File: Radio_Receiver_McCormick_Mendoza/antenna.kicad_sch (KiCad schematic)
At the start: 30 parts, among them J33 XFIL_IN, J34 XFIL_OUT, J5 Conn_Coaxial, J5 FIL_IN, J8 FIL_OUT, T1 Transformer_1P_SS, U13 SN74CBT3253CDBR

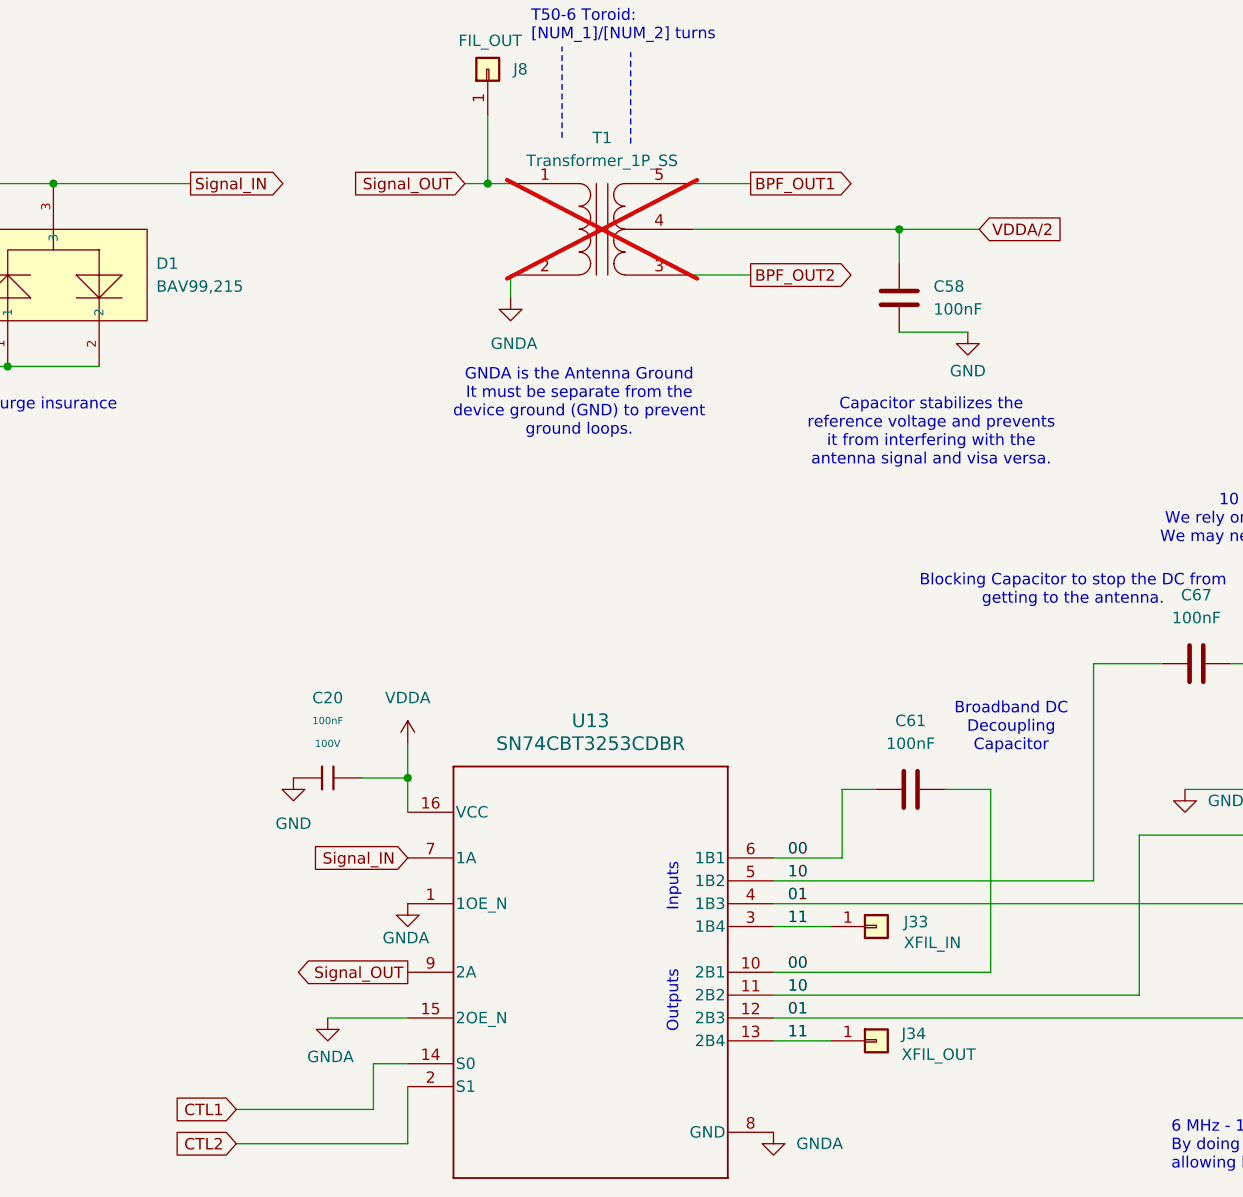
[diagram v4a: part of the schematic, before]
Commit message: Finalized Pico connections and added indicator LEDs
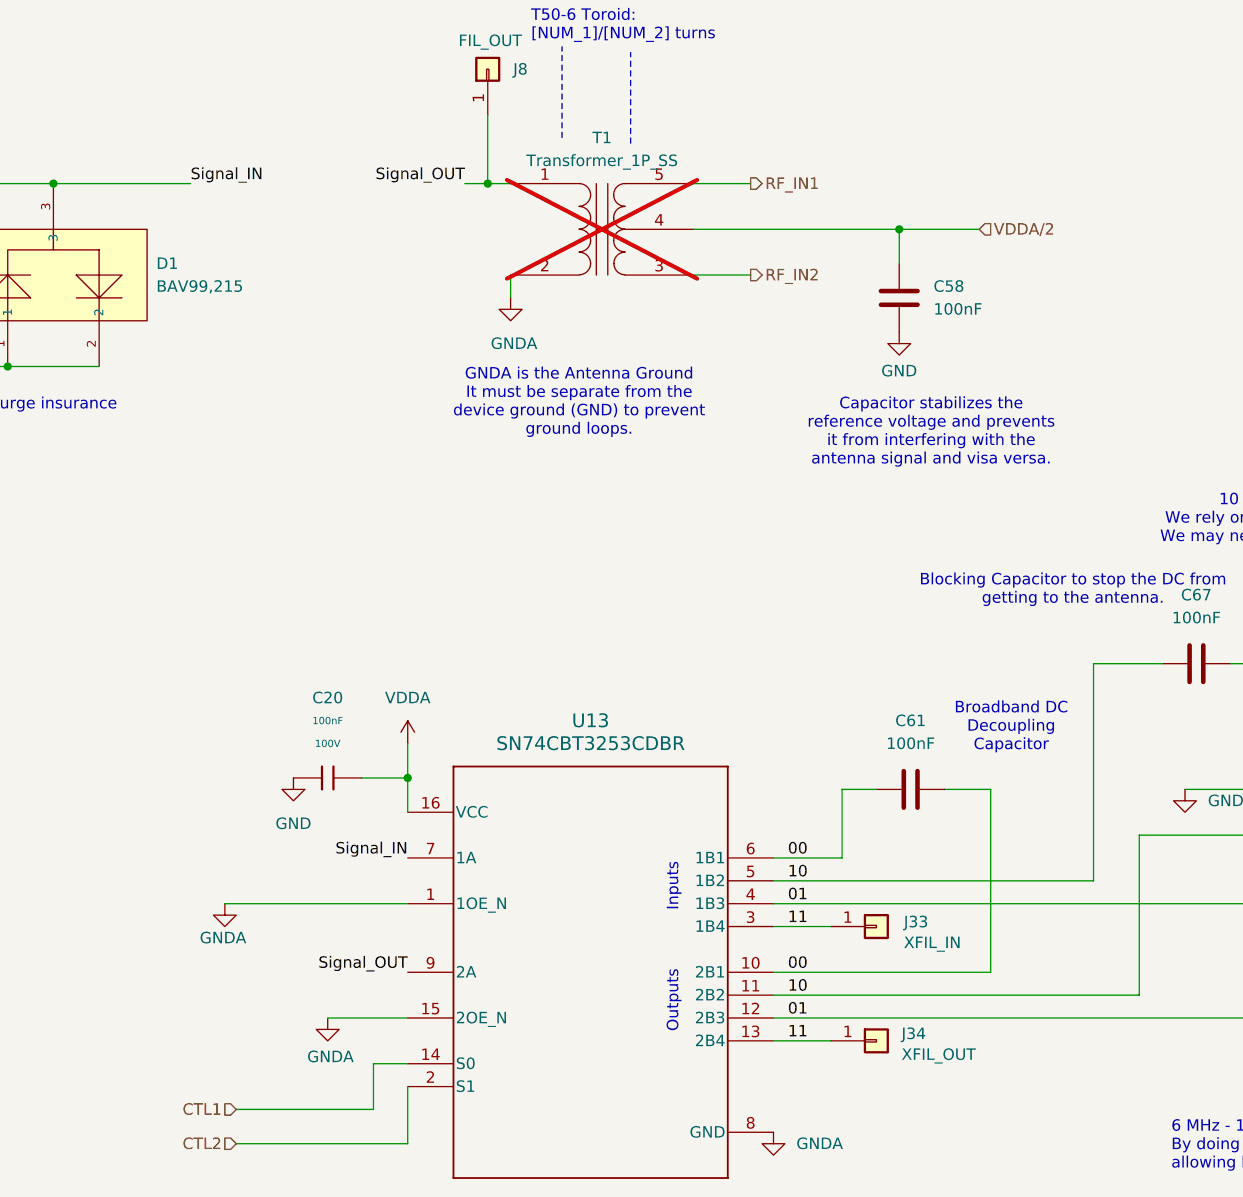
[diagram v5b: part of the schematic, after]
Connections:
- net BPF_OUT1 renamed RF_IN1
- net BPF_OUT2 renamed RF_IN2
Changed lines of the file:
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@@
 	(wire
 		(pts
+			(xy 86.36 120.65) (xy 106.68 120.65)
+		)
+		(stroke
+			(width 0)
+			(type default)
+		)
+	)
+	(wire
+		(pts
 			(xy 106.68 133.35) (xy 97.79 133.35)
 		)
@@
 	(wire
 		(pts
-			(xy 161.29 57.15) (xy 168.91 57.15)
-		)
-		(stroke
-			(width 0)
-			(type default)
-		)
-	)
-	(wire
-		(pts
 			(xy 198.12 93.98) (xy 203.2 93.98)
 		)
@@
 		)
 	)
-	(label "00"
-		(at 151.13 128.27 180)
+	(label "Signal_OUT"
+		(at 106.68 128.27 180)
 		(effects
 			(font
@@
 		)
 	)
-	(label "01"
-		(at 151.13 133.35 180)
+	(label "00"
+		(at 151.13 128.27 180)
 		(effects
 			(font
@@
 		)
 	)
-	(label "11"
-		(at 151.13 135.89 180)
+	(label "01"
+		(at 151.13 133.35 180)
 		(effects
 			(font
@@
 		)
 	)
-	(label "10"
-		(at 151.13 118.11 180)
+	(label "Signal_IN"
+		(at 106.68 115.57 180)
 		(effects
 			(font
@@
 		)
 	)
-	(label "00"
-		(at 151.13 115.57 180)
+	(label "11"
+		(at 151.13 135.89 180)
 		(effects
 			(font
@@
 	)
 	(label "10"
-		(at 151.13 130.81 180)
+		(at 151.13 118.11 180)
 		(effects
 			(font
@@
 		)
 	)
-	(label "01"
-		(at 151.13 120.65 180)
+	(label "00"
+		(at 151.13 115.57 180)
 		(effects
 			(font
@@
 		)
 	)
-	(global_label "CTL2"
-		(shape input)
-		(at 87.63 147.32 180)
-		(fields_autoplaced yes)
-		(effects
-			(font
-				(size 1.27 1.27)
-			)
-			(justify right)
-		)
-		(property "Intersheetrefs" "${INTERSHEET_REFS}"
-			(at 80.1696 147.32 0)
-			(hide yes)
-			(show_name no)
-			(do_not_autoplace no)
-			(effects
-				(font
-					(size 1.27 1.27)
-				)
-				(justify right)
-			)
-		)
-	)
-	(global_label "Signal_IN"
-		(shape input)
-		(at 106.68 115.57 180)
-		(fields_autoplaced yes)
+	(label "Signal_IN"
+		(at 82.55 40.64 0)
 		(effects
 			(font
 				(size 1.27 1.27)
 			)
-			(justify right)
-		)
-		(property "Intersheetrefs" "${INTERSHEET_REFS}"
-			(at 94.8654 115.57 0)
-			(hide yes)
-			(show_name no)
-			(do_not_autoplace no)
-			(effects
-				(font
-					(size 1.27 1.27)
-				)
-				(justify right)
-			)
+			(justify left bottom)
 		)
 	)
-	(global_label "Signal_OUT"
-		(shape input)
+	(label "Signal_OUT"
 		(at 113.03 40.64 180)
-		(fields_autoplaced yes)
 		(effects
 			(font
 				(size 1.27 1.27)
 			)
-			(justify right)
-		)
-		(property "Intersheetrefs" "${INTERSHEET_REFS}"
-			(at 99.5221 40.64 0)
-			(hide yes)
-			(show_name no)
-			(do_not_autoplace no)
-			(effects
-				(font
-					(size 1.27 1.27)
-				)
-				(justify right)
-			)
+			(justify right bottom)
 		)
 	)
-	(global_label "BPF_OUT2"
-		(shape output)
-		(at 144.78 50.8 0)
-		(fields_autoplaced yes)
+	(label "10"
+		(at 151.13 130.81 180)
 		(effects
 			(font
 				(size 1.27 1.27)
 			)
-			(justify left)
-		)
-		(property "Intersheetrefs" "${INTERSHEET_REFS}"
-			(at 157.1995 50.8 0)
-			(hide yes)
-			(show_name no)
-			(do_not_autoplace no)
-			(effects
-				(font
-					(size 1.27 1.27)
-				)
-				(justify left)
-			)
+			(justify right bottom)
 		)
 	)
-	(global_label "Signal_OUT"
-		(shape output)
-		(at 106.68 128.27 180)
-		(fields_autoplaced yes)
+	(label "01"
+		(at 151.13 120.65 180)
 		(effects
 			(font
 				(size 1.27 1.27)
 			)
-			(justify right)
-		)
-		(property "Intersheetrefs" "${INTERSHEET_REFS}"
-			(at 93.1721 128.27 0)
-			(hide yes)
-			(show_name no)
-			(do_not_autoplace no)
-			(effects
-				(font
-					(size 1.27 1.27)
-				)
-				(justify right)
-			)
+			(justify right bottom)
 		)
 	)
-	(global_label "Signal_IN"
+	(hierarchical_label "RF_IN1"
 		(shape output)
-		(at 82.55 40.64 0)
-		(fields_autoplaced yes)
+		(at 144.78 40.64 0)
 		(effects
 			(font
@@
 			(justify left)
 		)
-		(property "Intersheetrefs" "${INTERSHEET_REFS}"
-			(at 94.3646 40.64 0)
-			(hide yes)
-			(show_name no)
-			(do_not_autoplace no)
-			(effects
-				(font
-					(size 1.27 1.27)
-				)
-				(justify left)
-			)
-		)
 	)
-	(global_label "VDDA{slash}2"
+	(hierarchical_label "CTL2"
 		(shape input)
-		(at 170.18 45.72 0)
-		(fields_autoplaced yes)
+		(at 87.63 147.32 180)
 		(effects
 			(font
 				(size 1.27 1.27)
 			)
-			(justify left)
-		)
-		(property "Intersheetrefs" "${INTERSHEET_REFS}"
-			(at 180.4224 45.72 0)
-			(hide yes)
-			(show_name no)
-			(do_not_autoplace no)
-			(effects
-				(font
-					(size 1.27 1.27)
-				)
-				(justify left)
-			)
+			(justify right)
 		)
 	)
-	(global_label "CTL1"
+	(hierarchical_label "CTL1"
 		(shape input)
 		(at 87.63 143.51 180)
-		(fields_autoplaced yes)
 		(effects
 			(font
@@
 			(justify right)
 		)
-		(property "Intersheetrefs" "${INTERSHEET_REFS}"
-			(at 80.1696 143.51 0)
-			(hide yes)
-			(show_name no)
-			(do_not_autoplace no)
-			(effects
-				(font
-					(size 1.27 1.27)
-				)
-				(justify right)
+	)
+	(hierarchical_label "VDDA{slash}2"
+		(shape input)
+		(at 170.18 45.72 0)
+		(effects
+			(font
+				(size 1.27 1.27)
 			)
+			(justify left)
 		)
 	)
-	(global_label "BPF_OUT1"
+	(hierarchical_label "RF_IN2"
 		(shape output)
-		(at 144.78 40.64 0)
-		(fields_autoplaced yes)
+		(at 144.78 50.8 0)
 		(effects
 			(font
@@
 			(justify left)
 		)
-		(property "Intersheetrefs" "${INTERSHEET_REFS}"
-			(at 157.1995 40.64 0)
-			(hide yes)
-			(show_name no)
-			(do_not_autoplace no)
-			(effects
-				(font
-					(size 1.27 1.27)
-				)
-				(justify left)
-			)
-		)
 	)
 	(symbol
@@
 	(symbol
 		(lib_id "power:GND")
-		(at 168.91 57.15 0)
+		(at 161.29 57.15 0)
 		(unit 1)
 		(body_style 1)
@@
 		(dnp no)
 		(property "Reference" "#PWR063"
-			(at 168.91 63.5 0)
+			(at 161.29 63.5 0)
 			(hide yes)
 			(show_name no)
@@
 		)
 		(property "Value" "GND"
-			(at 168.91 61.468 0)
+			(at 161.29 61.468 0)
 			(show_name no)
 			(do_not_autoplace no)
@@
 		)
 		(property "Footprint" ""
-			(at 168.91 57.15 0)
+			(at 161.29 57.15 0)
 			(hide yes)
 			(show_name no)
@@
 		)
 		(property "Datasheet" ""
-			(at 168.91 57.15 0)
+			(at 161.29 57.15 0)
 			(hide yes)
 			(show_name no)
@@
 		)
 		(property "Description" "Power symbol creates a global label with name \"GND\" , ground"
-			(at 168.91 57.15 0)
+			(at 161.29 57.15 0)
 			(hide yes)
 			(show_name no)
@@
 	(symbol
 		(lib_id "power:GND")
-		(at 106.68 120.65 0)
+		(at 86.36 120.65 0)
 		(unit 1)
 		(body_style 1)
@@
 		(dnp no)
 		(property "Reference" "#PWR09"
-			(at 106.68 127 0)
+			(at 86.36 127 0)
 			(hide yes)
 			(show_name no)
@@
 		)
 		(property "Value" "GNDA"
-			(at 103.886 124.46 0)
+			(at 83.566 124.46 0)
 			(show_name no)
 			(do_not_autoplace no)
@@
 		)
 		(property "Footprint" ""
-			(at 106.68 120.65 0)
+			(at 86.36 120.65 0)
 			(hide yes)
 			(show_name no)
@@
 		)
 		(property "Datasheet" ""
-			(at 106.68 120.65 0)
+			(at 86.36 120.65 0)
 			(hide yes)
 			(show_name no)
@@
 		)
 		(property "Description" "Power symbol creates a global label with name \"GND\" , ground"
-			(at 106.68 120.65 0)
+			(at 86.36 120.65 0)
 			(hide yes)
 			(show_name no)

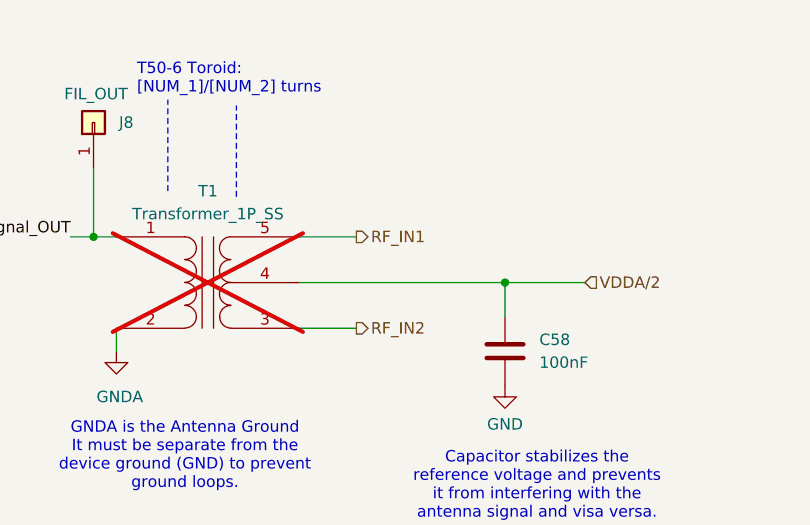
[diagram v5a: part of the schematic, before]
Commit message: Added transformer footprint and datasheet
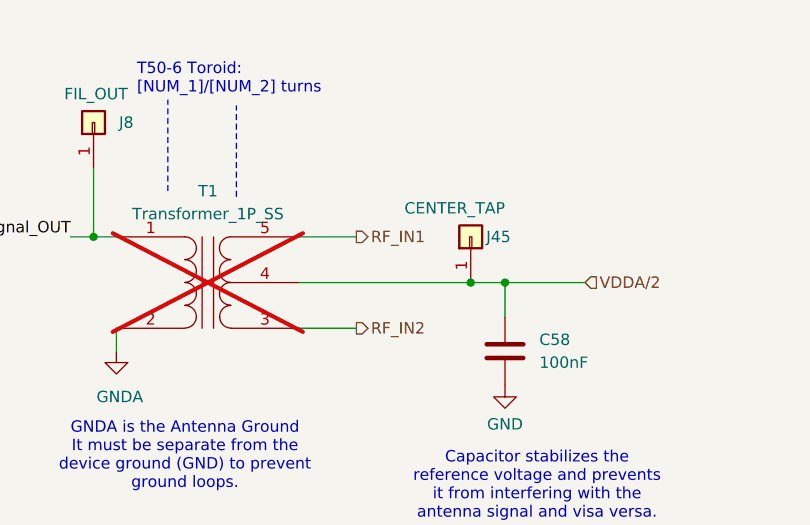
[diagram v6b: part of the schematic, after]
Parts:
- added J45: CENTER_TAP, Connector_PinHeader_2.54mm:PinHeader_1x01_P2.54mm_Vertical, symbol SDRReciever-rescue:Conn_01x01-Connector_Generic-SDRReciever-rescue
- C11, C19, C3, C4: Manufacturer FH(Guangdong Fenghua Advanced Tech) -> (none)
- C2, C22, C30, C31, C51, C53, C54, C55, C87: Manufacturer Samsung Electro-Mechanics -> (none)
- D1: Manufacturer Nexperia -> (none)
- T1: footprint (none) -> Reciever_Parts:Transformer_Toroid_Vertical_2Pri_3Sec_T37
- U13: LCSC (none) -> C2674583; Price (none) -> 3.5033USD
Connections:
- net VDDA/2: now also J45.1 (Pin_1)
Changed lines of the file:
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@@
 	)
 	(junction
+		(at 157.48 45.72)
+		(diameter 0)
+		(color 0 0 0 0)
+	)
+	(junction
 		(at 226.06 133.35)
 		(diameter 0)
@@
 	(wire
 		(pts
+			(xy 157.48 45.72) (xy 161.29 45.72)
+		)
+		(stroke
+			(width 0)
+			(type default)
+		)
+	)
+	(wire
+		(pts
 			(xy 250.19 132.08) (xy 250.19 133.35)
 		)
@@
 	(wire
 		(pts
-			(xy 138.43 45.72) (xy 161.29 45.72)
+			(xy 138.43 45.72) (xy 157.48 45.72)
 		)
 		(stroke
@@
 			)
 		)
-		(property "Footprint" ""
+		(property "Footprint" "Reciever_Parts:Transformer_Toroid_Vertical_2Pri_3Sec_T37"
 			(at 128.27 45.72 0)
 			(hide yes)
@@
 			)
 		)
-		(property "Datasheet" ""
+		(property "Datasheet" "https://www.rf-microwave.com/resources/products_attachments/6128ffba1982b.pdf"
 			(at 128.27 45.72 0)
 			(hide yes)
@@
 			)
 		)
-		(property "Manufacturer" "Samsung Electro-Mechanics"
-			(at 220.98 105.41 0)
-			(hide yes)
-			(show_name no)
-			(do_not_autoplace no)
-			(effects
-				(font
-					(size 1.27 1.27)
-				)
-			)
-		)
 		(property "Part" "CL21C222JBFNNNE"
 			(at 220.98 105.41 0)
@@
 			)
 		)
-		(property "Manufacturer" "FH(Guangdong Fenghua Advanced Tech)"
-			(at 242.57 97.79 0)
-			(hide yes)
-			(show_name no)
-			(do_not_autoplace no)
-			(effects
-				(font
-					(size 1.27 1.27)
-				)
-			)
-		)
 		(property "Part" "0402CG101J500NT"
 			(at 242.57 97.79 0)
@@
 			)
 		)
-		(property "Manufacturer" "Samsung Electro-Mechanics"
-			(at 220.98 97.79 0)
-			(hide yes)
-			(show_name no)
-			(do_not_autoplace no)
-			(effects
-				(font
-					(size 1.27 1.27)
-				)
-			)
-		)
 		(property "Part" "CL21C222JBFNNNE"
 			(at 220.98 97.79 0)
@@
 			)
 		)
-		(property "Manufacturer" "Samsung Electro-Mechanics"
-			(at 261.62 97.79 0)
-			(hide yes)
-			(show_name no)
-			(do_not_autoplace no)
-			(effects
-				(font
-					(size 1.27 1.27)
-				)
-			)
-		)
 		(property "Part" "CL21C222JBFNNNE"
 			(at 261.62 97.79 0)
@@
 			)
 		)
+		(property "LCSC" "C2674583"
+			(at 127 128.27 0)
+			(hide yes)
+			(show_name no)
+			(do_not_autoplace no)
+			(effects
+				(font
+					(size 1.27 1.27)
+				)
+			)
+		)
+		(property "Price" "3.5033USD"
+			(at 127 128.27 0)
+			(hide yes)
+			(show_name no)
+			(do_not_autoplace no)
+			(effects
+				(font
+					(size 1.27 1.27)
+				)
+			)
+		)
 		(pin "11"
 		)
@@
 			)
 		)
-		(property "Manufacturer" "Nexperia"
-			(at 67.31 50.8 0)
-			(hide yes)
-			(show_name no)
-			(do_not_autoplace no)
-			(effects
-				(font
-					(size 1.27 1.27)
-				)
-			)
-		)
 		(property "Part" "BAV99,215"
 			(at 67.31 50.8 0)
@@
 			)
 		)
-		(property "Manufacturer" "Samsung Electro-Mechanics"
-			(at 207.01 124.46 0)
-			(hide yes)
-			(show_name no)
-			(do_not_autoplace no)
-			(effects
-				(font
-					(size 1.27 1.27)
-				)
-			)
-		)
 		(property "Part" "CL10C331JB8NNNC"
 			(at 207.01 124.46 0)
@@
 			)
 		)
-		(property "Manufacturer" "FH(Guangdong Fenghua Advanced Tech)"
-			(at 233.68 128.27 0)
-			(hide yes)
-			(show_name no)
-			(do_not_autoplace no)
-			(effects
-				(font
-					(size 1.27 1.27)
-				)
-			)
-		)
 		(property "Part" "0402CG101J500NT"
 			(at 233.68 128.27 0)
@@
 			)
 		)
-		(property "Manufacturer" "Samsung Electro-Mechanics"
-			(at 224.79 128.27 0)
-			(hide yes)
-			(show_name no)
-			(do_not_autoplace no)
-			(effects
-				(font
-					(size 1.27 1.27)
-				)
-			)
-		)
 		(property "Part" "CL10C331JB8NNNC"
 			(at 224.79 128.27 0)
@@
 	)
 	(symbol
+		(lib_id "SDRReciever-rescue:Conn_01x01-Connector_Generic-SDRReciever-rescue")
+		(at 157.48 40.64 90)
+		(unit 1)
+		(body_style 1)
+		(exclude_from_sim no)
+		(in_bom yes)
+		(on_board yes)
+		(in_pos_files yes)
+		(dnp no)
+		(property "Reference" "J45"
+			(at 161.925 40.64 90)
+			(show_name no)
+			(do_not_autoplace no)
+			(effects
+				(font
+					(size 1.27 1.27)
+				)
+				(justify left)
+			)
+		)
+		(property "Value" "CENTER_TAP"
+			(at 161.29 37.465 90)
+			(show_name no)
+			(do_not_autoplace no)
+			(effects
+				(font
+					(size 1.27 1.27)
+				)
+				(justify left)
+			)
+		)
+		(property "Footprint" "Connector_PinHeader_2.54mm:PinHeader_1x01_P2.54mm_Vertical"
+			(at 157.48 40.64 0)
+			(hide yes)
+			(show_name no)
+			(do_not_autoplace no)
+			(effects
+				(font
+					(size 1.27 1.27)
+				)
+			)
+		)
+		(property "Datasheet" "~"
+			(at 157.48 40.64 0)
+			(hide yes)
+			(show_name no)
+			(do_not_autoplace no)
+			(effects
+				(font
+					(size 1.27 1.27)
+				)
+			)
+		)
+		(property "Description" ""
+			(at 157.48 40.64 0)
+			(show_name no)
+			(do_not_autoplace no)
+			(effects
+				(font
+					(size 1.27 1.27)
+				)
+			)
+		)
+		(pin "1"
+		)
+		(instances
+			(project "Radio_Receiver_McCormick_Mendoza"
+				(path "/f31d31ab-6846-4f3a-92b1-aa5a6a13373f/bb2f90fe-90d6-4041-8023-4e8a6153d0ef"
+					(reference "J45")
+					(unit 1)
+				)
+			)
+		)
+	)
+	(symbol
 		(lib_id "SDRReciever-rescue:Jumper_NC_Small-Device-SDRReciever-rescue")
 		(at 33.02 49.53 90)
@@
 			)
 		)
-		(property "Manufacturer" "Samsung Electro-Mechanics"
-			(at 261.62 105.41 0)
-			(hide yes)
-			(show_name no)
-			(do_not_autoplace no)
-			(effects
-				(font
-					(size 1.27 1.27)
-				)
-			)
-		)
 		(property "Part" "CL21C222JBFNNNE"
 			(at 261.62 105.41 0)
@@
 			)
 		)
-		(property "Manufacturer" "Samsung Electro-Mechanics"
-			(at 261.62 124.46 0)
-			(hide yes)
-			(show_name no)
-			(do_not_autoplace no)
-			(effects
-				(font
-					(size 1.27 1.27)
-				)
-			)
-		)
 		(property "Part" "CL10C331JB8NNNC"
 			(at 261.62 124.46 0)
@@
 			)
 		)
-		(property "Manufacturer" "Samsung Electro-Mechanics"
-			(at 212.09 97.79 0)
-			(hide yes)
-			(show_name no)
-			(do_not_autoplace no)
-			(effects
-				(font
-					(size 1.27 1.27)
-				)
-			)
-		)
 		(property "Part" "CL10C331JB8NNNC"
 			(at 212.09 97.79 0)
@@
 			)
 		)
-		(property "Manufacturer" "FH(Guangdong Fenghua Advanced Tech)"
-			(at 203.2 97.79 0)
-			(hide yes)
-			(show_name no)
-			(do_not_autoplace no)
-			(effects
-				(font
-					(size 1.27 1.27)
-				)
-			)
-		)
 		(property "Part" "0402CG101J500NT"
 			(at 203.2 97.79 0)
@@
 			)
 		)
-		(property "Manufacturer" "FH(Guangdong Fenghua Advanced Tech)"
-			(at 242.57 128.27 0)
-			(hide yes)
-			(show_name no)
-			(do_not_autoplace no)
-			(effects
-				(font
-					(size 1.27 1.27)
-				)
-			)
-		)
 		(property "Part" "0402CG101J500NT"
 			(at 242.57 128.27 0)
@@
 			(at 251.46 97.79 0)
 			(hide yes)
-			(show_name no)
-			(do_not_autoplace no)
-			(effects
-				(font
-					(size 1.27 1.27)
-				)
-			)
-		)
-		(property "Manufacturer" "Samsung Electro-Mechanics"
-			(at 251.46 97.79 0)
-			(hide yes)
